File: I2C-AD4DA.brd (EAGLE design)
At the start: 50 x 50 mm, 11 parts, among them IC1 PCF8591T, X1 RJ45-FRONT

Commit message: 1.1
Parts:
- added CA, CB, CC, CD: 0.1uF, SPCoast:0805-CAP
- added L1: 47 uH, rcl:L2012C
- added U$1: AGND+DGND, SPCoast:AGND+DGND
- C1: device SPCoast-minimal:0810-CAP -> SPCoast:UD-10X10_NICHICON
- C2: device SPCoast-minimal:0805-CAP -> SPCoast:0805-CAP
- I2C0, I2C1: value I2CLEFT -> CONNECTOR-I2CLEFT; device SPCoast-minimal:I2C-L -> SPCoast:I2C-L
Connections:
- new net N$1: IC1.14, L1.2
- net 5V: now also L1.1
- net AD0: now also CA.1
- net AD1: now also CB.1
- net AD2: now also CC.1
- net AD3: now also CD.1
- net AGND: now also CA.2, CB.2, CC.2, CD.2, IC1.13, U$1.AGND
- net GND: now also U$1.DGND; no longer IC1.13
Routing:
- net AD3: track 11.4 -> 21.8 mm
- net AD2: track 8.89 -> 15.8 mm
- net AD1: track 11.4 -> 16.0 mm
- net N$1: track 0.00 -> 3.13 mm
- net AGND: track 15.9 -> 13.5 mm, vias 0 -> 2
- net AD0: track 9.26 -> 11.4 mm
- net SDA: track 54.5 -> 55.1 mm
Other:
- board text added: "2014-10"
- board text added: "2014-12"
- board text added: "v1.1"
- board text removed: "2014-10 A"
- board text removed: "v1.0"

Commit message: 2.0
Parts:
- removed U$9: BOARD50X50, SPCoast-minimal:BOARD-SEEED5X5
- added BOARD1: (no value), SPCoast:BOARD-DINRAIL-3.17INX5CM
- added CON1, CON2: CONNECTOR-GROVE-4P-2.0-3470130P1, SPCoast:4P-2.0
- A0, A1, A2: device SPCoast-minimal:J3-254 -> SPCoast:J3-254
- IC1: device micro-philips:SO16W -> SPCoast:SO16W
- L1: device rcl:L2012C -> SPCoast:L2012C
- LOGO1: value OSHW-LOGOL -> DOC-OSHW-LOGO-L; device SPCoast-minimal:OSHW-LOGO-L -> SPCoast:OSHW-LOGO-L
- X1: value RJ45-FRONT -> (none); device SPCoast-minimal:RJ45-NO-SHIELD -> SPCoast:RJ45-NO-SHIELD
- moved C2 38.3 mm to (10.8, 66.0), turned to 180 degrees
- moved X1 37.5 mm to (22.2, 84.5)
- moved LOGO1 33.1 mm to (7.62, 77.5)
- moved CC 33.0 mm to (29.2, 58.4)
- moved CD 33.0 mm to (29.2, 55.9)
- moved CA 33.0 mm to (29.2, 63.5)
- moved CB 33.0 mm to (29.2, 61.0)
- moved C1 33.0 mm to (7.62, 58.4)
- moved IC1 33.0 mm to (21.0, 58.4)
- moved A0 33.0 mm to (27.9, 41.9)
- moved A1 33.0 mm to (25.4, 41.9)
- moved A2 33.0 mm to (22.9, 41.9)
- moved L1 33.0 mm to (24.1, 50.8)
- moved U$1 33.0 mm to (14.0, 57.8)
- moved I2C0 21.6 mm to (11.4, 35.6)
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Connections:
- new net VIN: CON1.3, CON1.4, CON2.3, CON2.4
- net GND: now also CON1.1, CON1.2, CON2.1, CON2.2
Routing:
- net VIN: track 0.00 -> 103.8 mm
- net GND: track 23.2 -> 34.1 mm, vias 2 -> 5
- net SDA: track 55.1 -> 61.2 mm
- net AD1: track 16.0 -> 21.0 mm
- net AD3: track 21.8 -> 26.7 mm
- net AD2: track 15.8 -> 20.7 mm
- net AD0: track 11.4 -> 15.9 mm
- net SCL: track 60.8 -> 64.2 mm
- net AGND: track 13.5 -> 15.5 mm
- net DA0: track 24.6 -> 26.4 mm, vias 2 -> 0
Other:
- board size 50 x 50 mm -> 56 x 100 mm
- board text added: "2018-07"
- board text added: "I2C-AD4DA"
- board text added: "Vin"
- board text added: "v2.0"
- board text removed: "2014-10"
- board text removed: "2014-12"
- board text removed: "v1.1"

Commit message: 3.0
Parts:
- removed X1: (no value), SPCoast:RJ45-NO-SHIELD
- added C3, C4: 0.1uF, SPCoast:0805-CAP
- added U$2, U$3, U$4, U$7: R-SLIDE-POT-45MM, SPCoast:SLIDER-45MM
- A0, A1, A2: device SPCoast:J3-254 -> SPCoast:SJ_3_PASTE1&2
- BOARD1: device SPCoast:BOARD-DINRAIL-3.17INX5CM -> SPCoast:BOARD-DINRAIL-3.17INX10CM
- moved CON2 49.1 mm to (91.4, 36.8)
- moved I2C1 48.9 mm to (87.6, 27.9)
- moved A0 10.2 mm to (27.9, 31.8)
- moved A1 10.2 mm to (25.4, 31.8)
- moved A2 10.2 mm to (22.9, 31.8)
- moved CON1 8.89 mm to (6.35, 36.8)
- moved I2C0 7.62 mm to (11.4, 27.9)
- moved CA 3.81 mm to (33.0, 63.5)
- moved CB 3.81 mm to (33.0, 61.0)
- moved CC 3.81 mm to (33.0, 58.4)
- moved CD 3.81 mm to (33.0, 55.9)
- moved L1 2.54 mm to (24.1, 48.3)
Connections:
- net 5V: now also C3.1, C4.1, U$2.E, U$3.E, U$4.E, U$7.E; no longer X1.1
- net AD0: now also U$7.S; no longer X1.2
- net AD1: now also U$4.S; no longer X1.3
- net AD2: now also U$3.S; no longer X1.4
- net AD3: now also U$2.S; no longer X1.5
- net AGND: now also C3.2, U$2.A, U$2.AGND@0, U$2.AGND@1, U$3.A, U$3.AGND@0, U$3.AGND@1, U$4.A, U$4.AGND@0, U$4.AGND@1, U$7.A, U$7.AGND@0, U$7.AGND@1; no longer X1.6
- net DA0: no longer X1.7
- net GND: now also C4.2; no longer X1.8
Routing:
- net SCL: track 64.2 -> 121.9 mm
- net SDA: track 61.2 -> 118.3 mm
- net AD3: track 26.7 -> 81.7 mm, vias 0 -> 2
- net AD2: track 20.7 -> 71.9 mm, vias 0 -> 2
- net AD1: track 21.0 -> 63.3 mm, vias 0 -> 2
- net VIN: track 103.8 -> 143.6 mm
- net AD0: track 15.9 -> 51.9 mm, vias 0 -> 2
- net GND: track 34.1 -> 63.4 mm
- net DA0: track 26.4 -> 0.00 mm
- net A2: track 23.2 -> 34.2 mm
- net A0: track 24.3 -> 34.9 mm
- net A1: track 23.7 -> 34.4 mm
- net AGND: track 15.5 -> 18.4 mm
- net N$1: track 3.13 -> 5.67 mm
- net 5V: track 5.08 -> 6.35 mm, vias 0 -> 3
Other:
- board size 56 x 100 mm -> 106 x 100 mm
- board text added: "2019-04"
- board text added: "LightUI"
- board text added: "R G B"
- board text added: "W"
- board text added: "v3.0"
- board text removed: "+5"
- board text removed: "2018-07"
- board text removed: "Agnd"
- board text removed: "DA0"
- board text removed: "Dgnd"
- board text removed: "I2C 4ch A/D 1ch D/A"
- board text removed: "v2.0"

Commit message: added values for connectors
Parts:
- A0, A1, A2: value (none) -> SJ
- BOARD1: value (none) -> 10x10
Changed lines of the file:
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@@
 <element name="I2C1" library="SPCoast" package="I2C-L" value="CONNECTOR-I2CLEFT" x="87.63" y="27.94" smashed="yes"/>
 <element name="I2C0" library="SPCoast" package="I2C-L" value="CONNECTOR-I2CLEFT" x="11.43" y="27.94" smashed="yes"/>
-<element name="A2" library="SPCoast" package="SJ_3_PASTE1&amp;2" value="" x="22.86" y="31.75" smashed="yes" rot="R90">
+<element name="A2" library="SPCoast" package="SJ_3_PASTE1&amp;2" value="SJ" x="22.86" y="31.75" smashed="yes" rot="R90">
 <attribute name="NAME" x="23.289" y="25.274" size="1.27" layer="51" ratio="10" rot="R90"/>
 <attribute name="VALUE" x="26.368" y="27.814" size="1.27" layer="27" ratio="10" rot="R90"/>
 </element>
-<element name="A1" library="SPCoast" package="SJ_3_PASTE1&amp;2" value="" x="25.4" y="31.75" smashed="yes" rot="R90">
+<element name="A1" library="SPCoast" package="SJ_3_PASTE1&amp;2" value="SJ" x="25.4" y="31.75" smashed="yes" rot="R90">
 <attribute name="NAME" x="25.829" y="25.274" size="1.27" layer="51" ratio="10" rot="R90"/>
 <attribute name="VALUE" x="28.908" y="27.814" size="1.27" layer="27" ratio="10" rot="R90"/>
 </element>
-<element name="A0" library="SPCoast" package="SJ_3_PASTE1&amp;2" value="" x="27.94" y="31.75" smashed="yes" rot="R90">
+<element name="A0" library="SPCoast" package="SJ_3_PASTE1&amp;2" value="SJ" x="27.94" y="31.75" smashed="yes" rot="R90">
 <attribute name="NAME" x="28.369" y="25.274" size="1.27" layer="51" ratio="10" rot="R90"/>
 <attribute name="VALUE" x="31.448" y="27.814" size="1.27" layer="27" ratio="10" rot="R90"/>
@@
 </element>
 <element name="U$1" library="SPCoast" package="AGND+DGND" value="AGND+DGND" x="13.97" y="57.785" rot="R180"/>
-<element name="BOARD1" library="SPCoast" package="BOARD-DINRAIL-3.17INX10CM" value="" x="0" y="0"/>
+<element name="BOARD1" library="SPCoast" package="BOARD-DINRAIL-3.17INX10CM" value="10x10" x="0" y="0"/>
 <element name="CON1" library="SPCoast" package="4P-2.0" value="CONNECTOR-GROVE-4P-2.0-3470130P1" x="6.35" y="36.83" smashed="yes" rot="R90">
 <attribute name="NAME" x="3.81" y="34.925" size="0.889" layer="25" font="vector" ratio="11" rot="R90"/>

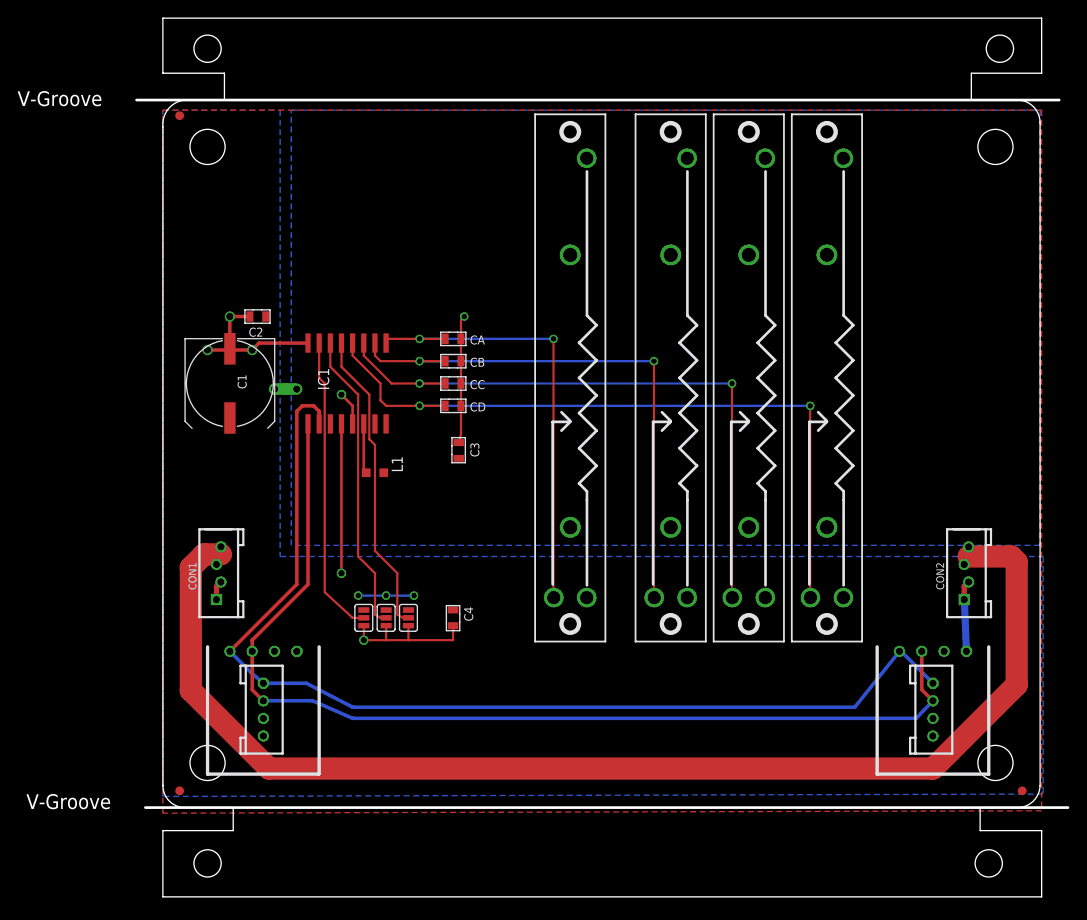
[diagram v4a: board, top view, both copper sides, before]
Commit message: normalized values
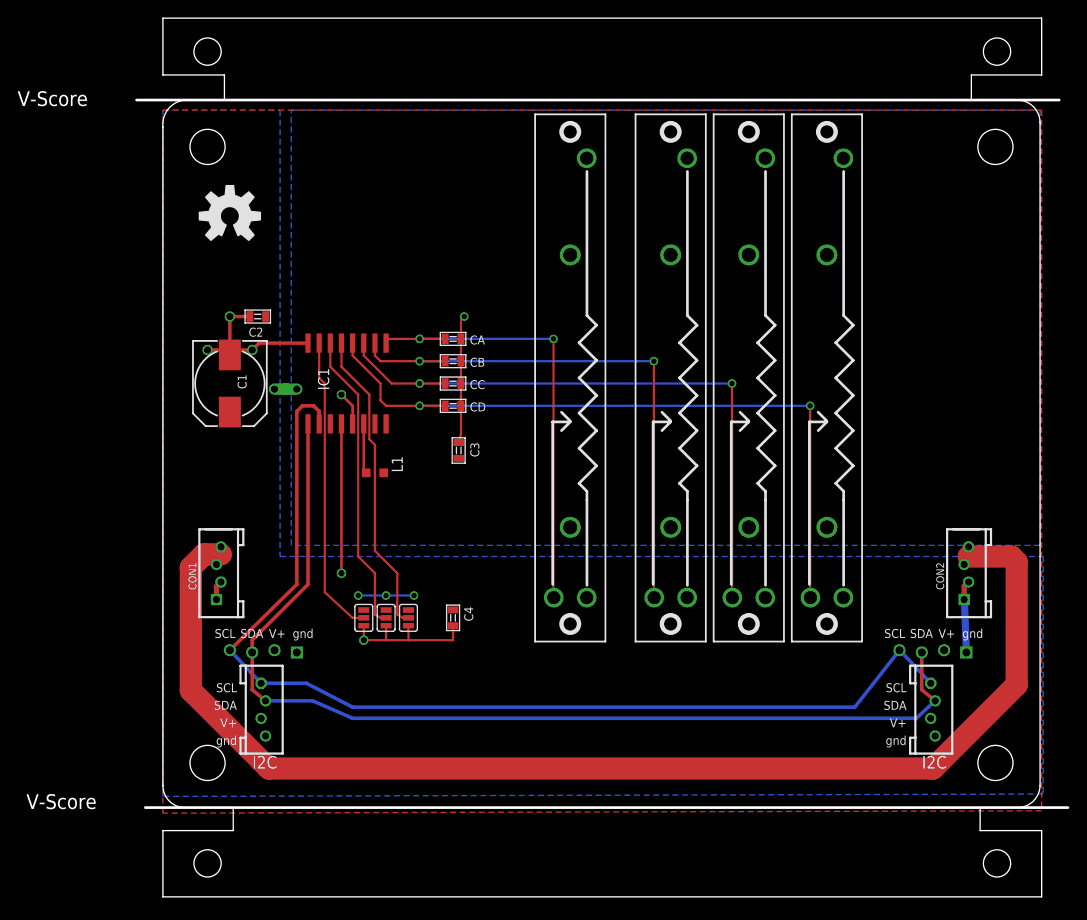
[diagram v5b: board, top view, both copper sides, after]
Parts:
- BOARD1: value 10x10 -> BOARD
- C1: value 150uF -> 220uF; device SPCoast:UD-10X10_NICHICON -> SPCoast:0810-CAP
- CON1, CON2: value CONNECTOR-GROVE-4P-2.0-3470130P1 -> 2mm
- I2C0, I2C1: value CONNECTOR-I2CLEFT -> I2C
- LOGO1: value DOC-OSHW-LOGO-L -> OSHW
- U$3, U$4, U$7: value R-SLIDE-POT-45MM -> (none)
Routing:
- net GND: track 63.4 -> 63.9 mm
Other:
- outline, holes or cut-outs redrawn
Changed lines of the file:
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@@
 </autorouter>
 <elements>
-<element name="C1" library="SPCoast" package="UD-10X10_NICHICON" value="150uF" x="7.62" y="58.42" smashed="yes" rot="R270">
+<element name="C1" library="SPCoast" package="0810-CAP" value="220uF" x="7.62" y="58.42" smashed="yes" rot="R270">
 <attribute name="NAME" x="9.525" y="57.785" size="1.016" layer="25" rot="R90"/>
 <attribute name="VALUE" x="5.08" y="60.325" size="1.016" layer="27" rot="R270"/>
@@
 <attribute name="VALUE" x="25.908" y="56.388" size="1.27" layer="27" rot="R180"/>
 </element>
-<element name="I2C1" library="SPCoast" package="I2C-L" value="CONNECTOR-I2CLEFT" x="87.63" y="27.94" smashed="yes"/>
-<element name="I2C0" library="SPCoast" package="I2C-L" value="CONNECTOR-I2CLEFT" x="11.43" y="27.94" smashed="yes"/>
+<element name="I2C1" library="SPCoast" package="I2C-L" value="I2C" x="87.63" y="27.94" smashed="yes"/>
+<element name="I2C0" library="SPCoast" package="I2C-L" value="I2C" x="11.43" y="27.94" smashed="yes"/>
 <element name="A2" library="SPCoast" package="SJ_3_PASTE1&amp;2" value="SJ" x="22.86" y="31.75" smashed="yes" rot="R90">
 <attribute name="NAME" x="23.289" y="25.274" size="1.27" layer="51" ratio="10" rot="R90"/>
@@
 <attribute name="VALUE" x="21.59" y="45.72" size="1.27" layer="27"/>
 </element>
-<element name="LOGO1" library="SPCoast" package="OSHW-LOGO-L" value="DOC-OSHW-LOGO-L" x="7.62" y="77.47"/>
+<element name="LOGO1" library="SPCoast" package="OSHW-LOGO-L" value="OSHW" x="7.62" y="77.47"/>
 <element name="C2" library="SPCoast" package="0805-CAP" value="0.1uF" x="10.795" y="66.04" smashed="yes" rot="R180">
 <attribute name="NAME" x="11.43" y="64.77" size="1.016" layer="25" rot="R180"/>
@@
 </element>
 <element name="U$1" library="SPCoast" package="AGND+DGND" value="AGND+DGND" x="13.97" y="57.785" rot="R180"/>
-<element name="BOARD1" library="SPCoast" package="BOARD-DINRAIL-3.17INX10CM" value="10x10" x="0" y="0"/>
-<element name="CON1" library="SPCoast" package="4P-2.0" value="CONNECTOR-GROVE-4P-2.0-3470130P1" x="6.35" y="36.83" smashed="yes" rot="R90">
+<element name="BOARD1" library="SPCoast" package="BOARD-DINRAIL-3.17INX10CM" value="BOARD" x="0" y="0"/>
+<element name="CON1" library="SPCoast" package="4P-2.0" value="2mm" x="6.35" y="36.83" smashed="yes" rot="R90">
 <attribute name="NAME" x="3.81" y="34.925" size="0.889" layer="25" font="vector" ratio="11" rot="R90"/>
 <attribute name="VALUE" x="-0.635" y="29.845" size="0.635" layer="27" font="vector" ratio="10" rot="R90"/>
 </element>
-<element name="CON2" library="SPCoast" package="4P-2.0" value="CONNECTOR-GROVE-4P-2.0-3470130P1" x="91.44" y="36.83" smashed="yes" rot="R90">
+<element name="CON2" library="SPCoast" package="4P-2.0" value="2mm" x="91.44" y="36.83" smashed="yes" rot="R90">
 <attribute name="NAME" x="88.9" y="34.925" size="0.889" layer="25" font="vector" ratio="11" rot="R90"/>
 <attribute name="VALUE" x="99.695" y="28.575" size="0.635" layer="27" font="vector" ratio="10" rot="R90"/>
 </element>
 <element name="U$2" library="SPCoast" package="SLIDER-45MM" value="R-SLIDE-POT-45MM" x="75.565" y="59.055" rot="R90"/>
-<element name="U$3" library="SPCoast" package="SLIDER-45MM" value="R-SLIDE-POT-45MM" x="66.675" y="59.055" rot="R90"/>
-<element name="U$4" library="SPCoast" package="SLIDER-45MM" value="R-SLIDE-POT-45MM" x="57.785" y="59.055" rot="R90"/>
-<element name="U$7" library="SPCoast" package="SLIDER-45MM" value="R-SLIDE-POT-45MM" x="46.355" y="59.055" rot="R90"/>
+<element name="U$3" library="SPCoast" package="SLIDER-45MM" value="" x="66.675" y="59.055" rot="R90"/>
+<element name="U$4" library="SPCoast" package="SLIDER-45MM" value="" x="57.785" y="59.055" rot="R90"/>
+<element name="U$7" library="SPCoast" package="SLIDER-45MM" value="" x="46.355" y="59.055" rot="R90"/>
 <element name="C3" library="SPCoast" package="0805-CAP" value="0.1uF" x="33.655" y="50.8" smashed="yes" rot="R90">
 <attribute name="NAME" x="36.0045" y="50.038" size="1.016" layer="25" rot="R90"/>
@@
 <via x="10.16" y="62.23" extent="1-16" drill="0.8" shape="square"/>
 <wire x1="5.08" y1="62.23" x2="7.48" y2="62.23" width="0.4064" layer="1"/>
-<wire x1="7.48" y1="62.23" x2="7.62" y2="62.37" width="0.4064" layer="1"/>
+<wire x1="7.48" y1="62.23" x2="7.62" y2="61.67" width="0.4064" layer="1"/>
 <wire x1="10.16" y1="62.23" x2="7.62" y2="62.23" width="0.4064" layer="1"/>
 <wire x1="7.62" y1="62.23" x2="7.62" y2="66.04" width="0.4064" layer="1"/>
@@
 <wire x1="33.02" y1="29.21" x2="27.94" y2="29.21" width="0.254" layer="1"/>
 <wire x1="91.186" y1="33.83" x2="91.186" y2="34.29" width="0.8128" layer="16"/>
-<wire x1="91.186" y1="34.29" x2="91.44" y2="27.94" width="0.8128" layer="16"/>
+<wire x1="91.186" y1="34.29" x2="91.44" y2="27.813" width="0.8128" layer="16"/>
 </signal>
 <signal name="A0">
@@
 <contactref element="I2C1" pad="SDA@1"/>
 <contactref element="I2C1" pad="SDA"/>
-<wire x1="10.16" y1="27.94" x2="10.16" y2="23.575" width="0.4064" layer="1"/>
-<wire x1="10.16" y1="23.575" x2="11.43" y2="22.305" width="0.4064" layer="1"/>
+<wire x1="10.16" y1="27.813" x2="10.16" y2="23.575" width="0.4064" layer="1"/>
+<wire x1="10.16" y1="23.575" x2="11.684" y2="22.305" width="0.4064" layer="1"/>
 <wire x1="16.51" y1="53.82" x2="16.51" y2="35.56" width="0.4064" layer="1"/>
 <wire x1="16.51" y1="35.56" x2="10.16" y2="29.21" width="0.4064" layer="1"/>
-<wire x1="10.16" y1="29.21" x2="10.16" y2="27.94" width="0.4064" layer="1"/>
-<wire x1="11.43" y1="22.305" x2="17.065" y2="22.305" width="0.4064" layer="16"/>
+<wire x1="10.16" y1="29.21" x2="10.16" y2="27.813" width="0.4064" layer="1"/>
+<wire x1="11.684" y1="22.305" x2="17.065" y2="22.305" width="0.4064" layer="16"/>
 <wire x1="17.065" y1="22.305" x2="21.59" y2="20.32" width="0.4064" layer="16"/>
 <wire x1="21.59" y1="20.32" x2="85.725" y2="20.32" width="0.4064" layer="16"/>
-<wire x1="85.725" y1="20.32" x2="87.63" y2="22.305" width="0.4064" layer="16"/>
-<wire x1="86.36" y1="27.94" x2="86.36" y2="23.575" width="0.4064" layer="1"/>
-<wire x1="86.36" y1="23.575" x2="87.63" y2="22.305" width="0.4064" layer="1"/>
+<wire x1="85.725" y1="20.32" x2="87.884" y2="22.305" width="0.4064" layer="16"/>
+<wire x1="86.36" y1="27.813" x2="86.36" y2="23.575" width="0.4064" layer="1"/>
+<wire x1="86.36" y1="23.575" x2="87.884" y2="22.305" width="0.4064" layer="1"/>
 </signal>
 <signal name="SCL">
@@
 <contactref element="I2C1" pad="SCL"/>
 <contactref element="I2C1" pad="SCL@1"/>
-<wire x1="7.62" y1="27.94" x2="9.985" y2="25.575" width="0.4064" layer="16"/>
-<wire x1="9.985" y1="25.575" x2="11.43" y2="24.305" width="0.4064" layer="16"/>
+<wire x1="7.62" y1="28.067" x2="9.985" y2="25.575" width="0.4064" layer="16"/>
+<wire x1="9.985" y1="25.575" x2="11.176" y2="24.305" width="0.4064" layer="16"/>
 <wire x1="15.875" y1="55.88" x2="15.24" y2="55.245" width="0.4064" layer="1"/>
 <wire x1="15.24" y1="55.245" x2="15.24" y2="35.56" width="0.4064" layer="1"/>
-<wire x1="15.24" y1="35.56" x2="7.62" y2="27.94" width="0.4064" layer="1"/>
-<wire x1="11.43" y1="24.305" x2="16.335" y2="24.305" width="0.4064" layer="16"/>
+<wire x1="15.24" y1="35.56" x2="7.62" y2="28.067" width="0.4064" layer="1"/>
+<wire x1="11.176" y1="24.305" x2="16.335" y2="24.305" width="0.4064" layer="16"/>
 <wire x1="16.335" y1="24.305" x2="21.59" y2="21.59" width="0.4064" layer="16"/>
 <wire x1="21.59" y1="21.59" x2="78.74" y2="21.59" width="0.4064" layer="16"/>
-<wire x1="78.74" y1="21.59" x2="83.82" y2="27.94" width="0.4064" layer="16"/>
-<wire x1="83.82" y1="28.115" x2="87.63" y2="24.305" width="0.4064" layer="16"/>
-<wire x1="83.82" y1="28.115" x2="83.82" y2="27.94" width="0.4064" layer="16"/>
+<wire x1="78.74" y1="21.59" x2="83.82" y2="28.067" width="0.4064" layer="16"/>
+<wire x1="83.82" y1="28.115" x2="87.376" y2="24.305" width="0.4064" layer="16"/>
+<wire x1="83.82" y1="28.115" x2="83.82" y2="28.067" width="0.4064" layer="16"/>
 </signal>
 <signal name="DA0">

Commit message: normalized values
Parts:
- U$2: value R-SLIDE-POT-45MM -> 10K
- U$3, U$4, U$7: value (none) -> 10K
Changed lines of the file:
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@@
 <attribute name="VALUE" x="99.695" y="28.575" size="0.635" layer="27" font="vector" ratio="10" rot="R90"/>
 </element>
-<element name="U$2" library="SPCoast" package="SLIDER-45MM" value="R-SLIDE-POT-45MM" x="75.565" y="59.055" rot="R90"/>
-<element name="U$3" library="SPCoast" package="SLIDER-45MM" value="" x="66.675" y="59.055" rot="R90"/>
-<element name="U$4" library="SPCoast" package="SLIDER-45MM" value="" x="57.785" y="59.055" rot="R90"/>
-<element name="U$7" library="SPCoast" package="SLIDER-45MM" value="" x="46.355" y="59.055" rot="R90"/>
+<element name="U$2" library="SPCoast" package="SLIDER-45MM" value="10K" x="75.565" y="59.055" rot="R90"/>
+<element name="U$3" library="SPCoast" package="SLIDER-45MM" value="10K" x="66.675" y="59.055" rot="R90"/>
+<element name="U$4" library="SPCoast" package="SLIDER-45MM" value="10K" x="57.785" y="59.055" rot="R90"/>
+<element name="U$7" library="SPCoast" package="SLIDER-45MM" value="10K" x="46.355" y="59.055" rot="R90"/>
 <element name="C3" library="SPCoast" package="0805-CAP" value="0.1uF" x="33.655" y="50.8" smashed="yes" rot="R90">
 <attribute name="NAME" x="36.0045" y="50.038" size="1.016" layer="25" rot="R90"/>
